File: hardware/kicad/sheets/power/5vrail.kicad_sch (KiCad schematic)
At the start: 11 parts, among them U8 TPSM33625RDNR

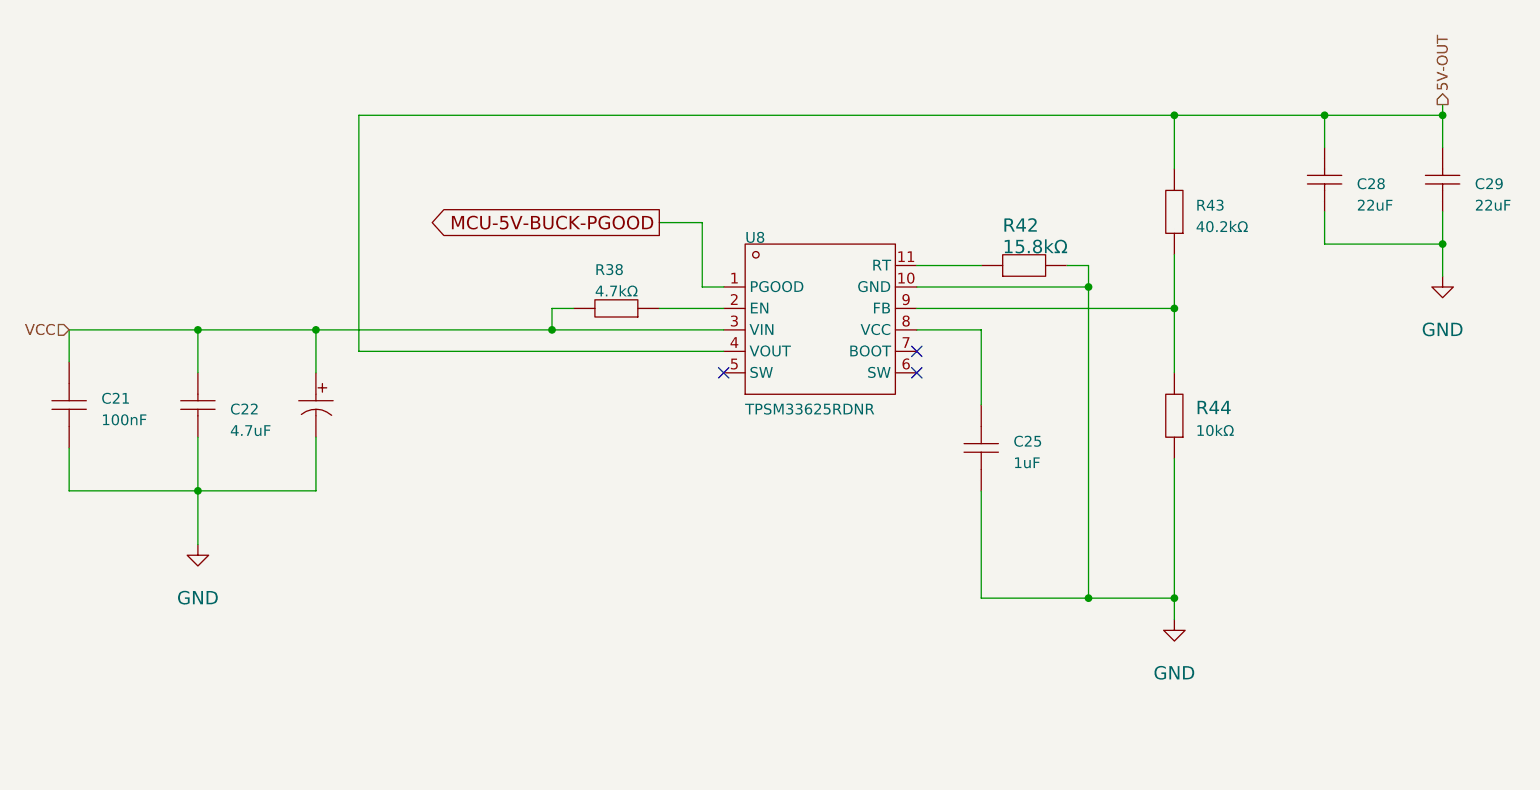
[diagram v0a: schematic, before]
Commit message: resheeted bms and fixed links for the 12v buck
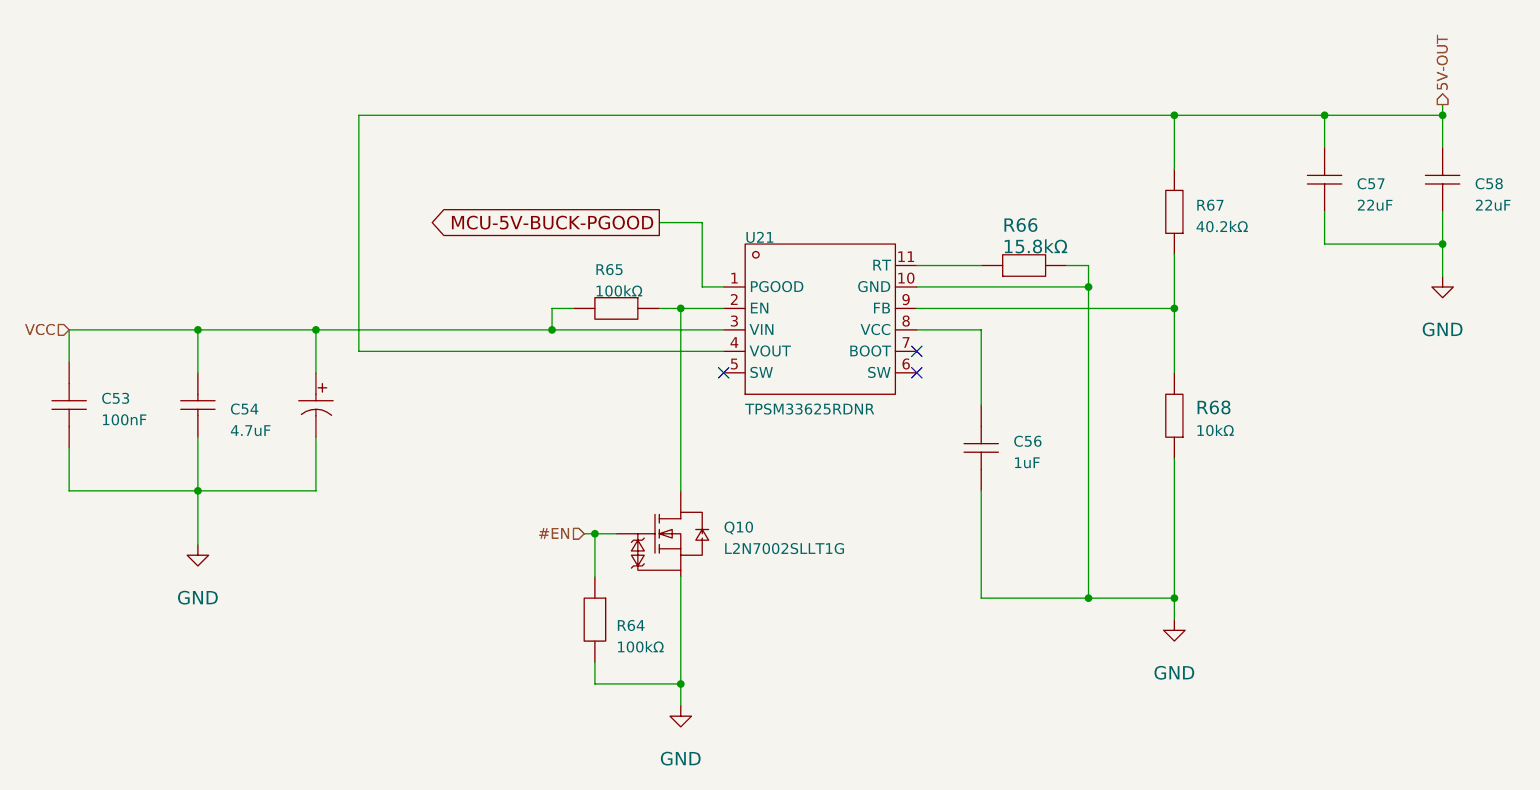
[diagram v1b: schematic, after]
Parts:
- removed R38: 4.7kΩ, Resistor_SMD:R_0603_1608Metric, symbol 5v rail sm-easyedapro:0603WAF4701T5E
- added Q10: L2N7002SLLT1G, Package_TO_SOT_SMD:SOT-23, symbol 5v rail sm-easyedapro:L2N7002SLLT1G
- added R64, R65: 100kΩ, Resistor_SMD:R_0603_1608Metric, symbol 5v rail sm-easyedapro:FRC0603J104 TS
- renumbered C21 to C53, C22 to C54, C23 to C55, C25 to C56, C28 to C57, C29 to C58, R42 to R66, R43 to R67, R44 to R68, U8 to U21
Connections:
- net GND: now also Q10.2 (S), R64.2
- net VCC: now also R65.2
- net at U21.2 (EN): now also Q10.3 (D), R65.1
- new net #EN: Q10.1 (G), R64.1

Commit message: realized having 2 3v3 rails can cause issues
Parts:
- renumbered C53 to C58, C54 to C59, C55 to C60, C56 to C61, C57 to C62, C58 to C63, Q10 to Q2, R64 to R66, R65 to R67, R66 to R68, R67 to R69, R68 to R70, U21 to U23
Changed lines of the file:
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@@
 		(on_board yes)
 		(dnp no)
-		(property "Reference" "C58"
+		(property "Reference" "C63"
 			(at 215.9 68.58 90)
 			(effects
@@
 		(instances
 			(project "svea_powerboard_rev3"
-				(path "/3f85abf4-0b95-4c4a-b7e9-06f59ca1ea3d/5c2e021f-c2d4-49e2-8c36-9a64f1f12002/a68287e1-0132-459f-8ffe-0b4658425697"
-					(reference "C58")
+				(path "/3f85abf4-0b95-4c4a-b7e9-06f59ca1ea3d/5c2e021f-c2d4-49e2-8c36-9a64f1f12001/de8125f2-04ec-46c6-89d6-d0b5e89f6023"
+					(reference "C63")
 					(unit 1)
 				)
@@
 		(on_board yes)
 		(dnp no)
-		(property "Reference" "U21"
+		(property "Reference" "U23"
 			(at 129.54 74.93 0)
 			(effects
@@
 		(instances
 			(project "svea_powerboard_rev3"
-				(path "/3f85abf4-0b95-4c4a-b7e9-06f59ca1ea3d/5c2e021f-c2d4-49e2-8c36-9a64f1f12002/a68287e1-0132-459f-8ffe-0b4658425697"
-					(reference "U21")
+				(path "/3f85abf4-0b95-4c4a-b7e9-06f59ca1ea3d/5c2e021f-c2d4-49e2-8c36-9a64f1f12001/de8125f2-04ec-46c6-89d6-d0b5e89f6023"
+					(reference "U23")
 					(unit 1)
 				)
@@
 		(on_board yes)
 		(dnp no)
-		(property "Reference" "R64"
+		(property "Reference" "R66"
 			(at 114.3 119.38 90)
 			(effects
@@
 		(instances
 			(project "svea_powerboard_rev3"
-				(path "/3f85abf4-0b95-4c4a-b7e9-06f59ca1ea3d/5c2e021f-c2d4-49e2-8c36-9a64f1f12002/a68287e1-0132-459f-8ffe-0b4658425697"
-					(reference "R64")
+				(path "/3f85abf4-0b95-4c4a-b7e9-06f59ca1ea3d/5c2e021f-c2d4-49e2-8c36-9a64f1f12001/de8125f2-04ec-46c6-89d6-d0b5e89f6023"
+					(reference "R66")
 					(unit 1)
 				)
@@
 		(on_board yes)
 		(dnp no)
-		(property "Reference" "Q10"
+		(property "Reference" "Q2"
 			(at 127 109.22 0)
 			(effects
@@
 		(instances
 			(project "svea_powerboard_rev3"
-				(path "/3f85abf4-0b95-4c4a-b7e9-06f59ca1ea3d/5c2e021f-c2d4-49e2-8c36-9a64f1f12002/a68287e1-0132-459f-8ffe-0b4658425697"
-					(reference "Q10")
+				(path "/3f85abf4-0b95-4c4a-b7e9-06f59ca1ea3d/5c2e021f-c2d4-49e2-8c36-9a64f1f12001/de8125f2-04ec-46c6-89d6-d0b5e89f6023"
+					(reference "Q2")
 					(unit 1)
 				)
@@
 		(on_board yes)
 		(dnp no)
-		(property "Reference" "#PWR075"
+		(property "Reference" "#PWR013"
 			(at 212.09 78.74 0)
 			(effects
@@
 		(instances
 			(project "svea_powerboard_rev3"
-				(path "/3f85abf4-0b95-4c4a-b7e9-06f59ca1ea3d/5c2e021f-c2d4-49e2-8c36-9a64f1f12002/a68287e1-0132-459f-8ffe-0b4658425697"
-					(reference "#PWR075")
+				(path "/3f85abf4-0b95-4c4a-b7e9-06f59ca1ea3d/5c2e021f-c2d4-49e2-8c36-9a64f1f12001/de8125f2-04ec-46c6-89d6-d0b5e89f6023"
+					(reference "#PWR013")
 					(unit 1)
 				)
@@
 		(on_board yes)
 		(dnp no)
-		(property "Reference" "C53"
+		(property "Reference" "C58"
 			(at 53.34 93.98 90)
 			(effects
@@
 		(instances
 			(project "svea_powerboard_rev3"
-				(path "/3f85abf4-0b95-4c4a-b7e9-06f59ca1ea3d/5c2e021f-c2d4-49e2-8c36-9a64f1f12002/a68287e1-0132-459f-8ffe-0b4658425697"
-					(reference "C53")
+				(path "/3f85abf4-0b95-4c4a-b7e9-06f59ca1ea3d/5c2e021f-c2d4-49e2-8c36-9a64f1f12001/de8125f2-04ec-46c6-89d6-d0b5e89f6023"
+					(reference "C58")
 					(unit 1)
 				)
@@
 		(on_board yes)
 		(dnp no)
-		(property "Reference" "R67"
+		(property "Reference" "R69"
 			(at 182.88 71.12 90)
 			(effects
@@
 		(instances
 			(project "svea_powerboard_rev3"
-				(path "/3f85abf4-0b95-4c4a-b7e9-06f59ca1ea3d/5c2e021f-c2d4-49e2-8c36-9a64f1f12002/a68287e1-0132-459f-8ffe-0b4658425697"
-					(reference "R67")
+				(path "/3f85abf4-0b95-4c4a-b7e9-06f59ca1ea3d/5c2e021f-c2d4-49e2-8c36-9a64f1f12001/de8125f2-04ec-46c6-89d6-d0b5e89f6023"
+					(reference "R69")
 					(unit 1)
 				)
@@
 		(on_board yes)
 		(dnp no)
-		(property "Reference" "C56"
+		(property "Reference" "C61"
 			(at 161.29 99.06 90)
 			(effects
@@
 		(instances
 			(project "svea_powerboard_rev3"
-				(path "/3f85abf4-0b95-4c4a-b7e9-06f59ca1ea3d/5c2e021f-c2d4-49e2-8c36-9a64f1f12002/a68287e1-0132-459f-8ffe-0b4658425697"
-					(reference "C56")
+				(path "/3f85abf4-0b95-4c4a-b7e9-06f59ca1ea3d/5c2e021f-c2d4-49e2-8c36-9a64f1f12001/de8125f2-04ec-46c6-89d6-d0b5e89f6023"
+					(reference "C61")
 					(unit 1)
 				)
@@
 		(on_board yes)
 		(dnp no)
-		(property "Reference" "#PWR074"
+		(property "Reference" "#PWR012"
 			(at 180.34 119.38 0)
 			(effects
@@
 		(instances
 			(project "svea_powerboard_rev3"
-				(path "/3f85abf4-0b95-4c4a-b7e9-06f59ca1ea3d/5c2e021f-c2d4-49e2-8c36-9a64f1f12002/a68287e1-0132-459f-8ffe-0b4658425697"
-					(reference "#PWR074")
+				(path "/3f85abf4-0b95-4c4a-b7e9-06f59ca1ea3d/5c2e021f-c2d4-49e2-8c36-9a64f1f12001/de8125f2-04ec-46c6-89d6-d0b5e89f6023"
+					(reference "#PWR012")
 					(unit 1)
 				)
@@
 		(on_board yes)
 		(dnp no)
-		(property "Reference" "#PWR073"
+		(property "Reference" "#PWR011"
 			(at 121.92 129.54 0)
 			(effects
@@
 		(instances
 			(project "svea_powerboard_rev3"
-				(path "/3f85abf4-0b95-4c4a-b7e9-06f59ca1ea3d/5c2e021f-c2d4-49e2-8c36-9a64f1f12002/a68287e1-0132-459f-8ffe-0b4658425697"
-					(reference "#PWR073")
+				(path "/3f85abf4-0b95-4c4a-b7e9-06f59ca1ea3d/5c2e021f-c2d4-49e2-8c36-9a64f1f12001/de8125f2-04ec-46c6-89d6-d0b5e89f6023"
+					(reference "#PWR011")
 					(unit 1)
 				)
@@
 		(on_board yes)
 		(dnp no)
-		(property "Reference" "R66"
+		(property "Reference" "R68"
 			(at 160.02 73.66 0)
 			(effects
@@
 		(instances
 			(project "svea_powerboard_rev3"
-				(path "/3f85abf4-0b95-4c4a-b7e9-06f59ca1ea3d/5c2e021f-c2d4-49e2-8c36-9a64f1f12002/a68287e1-0132-459f-8ffe-0b4658425697"
-					(reference "R66")
+				(path "/3f85abf4-0b95-4c4a-b7e9-06f59ca1ea3d/5c2e021f-c2d4-49e2-8c36-9a64f1f12001/de8125f2-04ec-46c6-89d6-d0b5e89f6023"
+					(reference "R68")
 					(unit 1)
 				)
@@
 		(on_board yes)
 		(dnp no)
-		(property "Reference" "R65"
+		(property "Reference" "R67"
 			(at 111.76 78.74 0)
 			(effects
@@
 		(instances
 			(project "svea_powerboard_rev3"
-				(path "/3f85abf4-0b95-4c4a-b7e9-06f59ca1ea3d/5c2e021f-c2d4-49e2-8c36-9a64f1f12002/a68287e1-0132-459f-8ffe-0b4658425697"
-					(reference "R65")
+				(path "/3f85abf4-0b95-4c4a-b7e9-06f59ca1ea3d/5c2e021f-c2d4-49e2-8c36-9a64f1f12001/de8125f2-04ec-46c6-89d6-d0b5e89f6023"
+					(reference "R67")
 					(unit 1)
 				)
@@
 		(on_board yes)
 		(dnp no)
-		(property "Reference" "C57"
+		(property "Reference" "C62"
 			(at 201.93 68.58 90)
 			(effects
@@
 		(instances
 			(project "svea_powerboard_rev3"
-				(path "/3f85abf4-0b95-4c4a-b7e9-06f59ca1ea3d/5c2e021f-c2d4-49e2-8c36-9a64f1f12002/a68287e1-0132-459f-8ffe-0b4658425697"
-					(reference "C57")
+				(path "/3f85abf4-0b95-4c4a-b7e9-06f59ca1ea3d/5c2e021f-c2d4-49e2-8c36-9a64f1f12001/de8125f2-04ec-46c6-89d6-d0b5e89f6023"
+					(reference "C62")
 					(unit 1)
 				)
@@
 		(on_board yes)
 		(dnp no)
-		(property "Reference" "C54"
+		(property "Reference" "C59"
 			(at 68.58 95.25 90)
 			(effects
@@
 		(instances
 			(project "svea_powerboard_rev3"
-				(path "/3f85abf4-0b95-4c4a-b7e9-06f59ca1ea3d/5c2e021f-c2d4-49e2-8c36-9a64f1f12002/a68287e1-0132-459f-8ffe-0b4658425697"
-					(reference "C54")
+				(path "/3f85abf4-0b95-4c4a-b7e9-06f59ca1ea3d/5c2e021f-c2d4-49e2-8c36-9a64f1f12001/de8125f2-04ec-46c6-89d6-d0b5e89f6023"
+					(reference "C59")
 					(unit 1)
 				)
@@
 		(on_board yes)
 		(dnp no)
-		(property "Reference" "#PWR072"
+		(property "Reference" "#PWR09"
 			(at 64.77 110.49 0)
 			(effects
@@
 		(instances
 			(project "svea_powerboard_rev3"
-				(path "/3f85abf4-0b95-4c4a-b7e9-06f59ca1ea3d/5c2e021f-c2d4-49e2-8c36-9a64f1f12002/a68287e1-0132-459f-8ffe-0b4658425697"
-					(reference "#PWR072")
+				(path "/3f85abf4-0b95-4c4a-b7e9-06f59ca1ea3d/5c2e021f-c2d4-49e2-8c36-9a64f1f12001/de8125f2-04ec-46c6-89d6-d0b5e89f6023"
+					(reference "#PWR09")
 					(unit 1)
 				)
@@
 		(on_board yes)
 		(dnp no)
-		(property "Reference" "R68"
+		(property "Reference" "R70"
 			(at 182.88 95.25 90)
 			(effects
@@
 		(instances
 			(project "svea_powerboard_rev3"
-				(path "/3f85abf4-0b95-4c4a-b7e9-06f59ca1ea3d/5c2e021f-c2d4-49e2-8c36-9a64f1f12002/a68287e1-0132-459f-8ffe-0b4658425697"
-					(reference "R68")
+				(path "/3f85abf4-0b95-4c4a-b7e9-06f59ca1ea3d/5c2e021f-c2d4-49e2-8c36-9a64f1f12001/de8125f2-04ec-46c6-89d6-d0b5e89f6023"
+					(reference "R70")
 					(unit 1)
 				)
@@
 		(on_board yes)
 		(dnp no)
-		(property "Reference" "C55"
+		(property "Reference" "C60"
 			(at 82.55 93.98 90)
 			(effects
@@
 		(instances
 			(project "svea_powerboard_rev3"
-				(path "/3f85abf4-0b95-4c4a-b7e9-06f59ca1ea3d/5c2e021f-c2d4-49e2-8c36-9a64f1f12002/a68287e1-0132-459f-8ffe-0b4658425697"
-					(reference "C55")
+				(path "/3f85abf4-0b95-4c4a-b7e9-06f59ca1ea3d/5c2e021f-c2d4-49e2-8c36-9a64f1f12001/de8125f2-04ec-46c6-89d6-d0b5e89f6023"
+					(reference "C60")
 					(unit 1)
 				)

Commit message: various improvements
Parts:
- renumbered C58 to C82, C59 to C83, C60 to C84, C61 to C85, C62 to C86, C63 to C87, Q2 to Q16, R66 to R90, R67 to R91, R68 to R92, R69 to R93, R70 to R94, U23 to U44
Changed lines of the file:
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@@
 		(on_board yes)
 		(dnp no)
-		(property "Reference" "C63"
+		(property "Reference" "C87"
 			(at 215.9 68.58 90)
 			(effects
@@
 			(project "svea_powerboard_rev3"
 				(path "/3f85abf4-0b95-4c4a-b7e9-06f59ca1ea3d/5c2e021f-c2d4-49e2-8c36-9a64f1f12001/de8125f2-04ec-46c6-89d6-d0b5e89f6023"
-					(reference "C63")
+					(reference "C87")
 					(unit 1)
 				)
@@
 		(on_board yes)
 		(dnp no)
-		(property "Reference" "U23"
+		(property "Reference" "U44"
 			(at 129.54 74.93 0)
 			(effects
@@
 			(project "svea_powerboard_rev3"
 				(path "/3f85abf4-0b95-4c4a-b7e9-06f59ca1ea3d/5c2e021f-c2d4-49e2-8c36-9a64f1f12001/de8125f2-04ec-46c6-89d6-d0b5e89f6023"
-					(reference "U23")
+					(reference "U44")
 					(unit 1)
 				)
@@
 		(on_board yes)
 		(dnp no)
-		(property "Reference" "R66"
+		(property "Reference" "R90"
 			(at 114.3 119.38 90)
 			(effects
@@
 			(project "svea_powerboard_rev3"
 				(path "/3f85abf4-0b95-4c4a-b7e9-06f59ca1ea3d/5c2e021f-c2d4-49e2-8c36-9a64f1f12001/de8125f2-04ec-46c6-89d6-d0b5e89f6023"
-					(reference "R66")
+					(reference "R90")
 					(unit 1)
 				)
@@
 		(on_board yes)
 		(dnp no)
-		(property "Reference" "Q2"
+		(property "Reference" "Q16"
 			(at 127 109.22 0)
 			(effects
@@
 			(project "svea_powerboard_rev3"
 				(path "/3f85abf4-0b95-4c4a-b7e9-06f59ca1ea3d/5c2e021f-c2d4-49e2-8c36-9a64f1f12001/de8125f2-04ec-46c6-89d6-d0b5e89f6023"
-					(reference "Q2")
+					(reference "Q16")
 					(unit 1)
 				)
@@
 		(on_board yes)
 		(dnp no)
-		(property "Reference" "#PWR013"
+		(property "Reference" "#PWR0139"
 			(at 212.09 78.74 0)
 			(effects
@@
 			(project "svea_powerboard_rev3"
 				(path "/3f85abf4-0b95-4c4a-b7e9-06f59ca1ea3d/5c2e021f-c2d4-49e2-8c36-9a64f1f12001/de8125f2-04ec-46c6-89d6-d0b5e89f6023"
-					(reference "#PWR013")
+					(reference "#PWR0139")
 					(unit 1)
 				)
@@
 		(on_board yes)
 		(dnp no)
-		(property "Reference" "C58"
+		(property "Reference" "C82"
 			(at 53.34 93.98 90)
 			(effects
@@
 			(project "svea_powerboard_rev3"
 				(path "/3f85abf4-0b95-4c4a-b7e9-06f59ca1ea3d/5c2e021f-c2d4-49e2-8c36-9a64f1f12001/de8125f2-04ec-46c6-89d6-d0b5e89f6023"
-					(reference "C58")
+					(reference "C82")
 					(unit 1)
 				)
@@
 		(on_board yes)
 		(dnp no)
-		(property "Reference" "R69"
+		(property "Reference" "R93"
 			(at 182.88 71.12 90)
 			(effects
@@
 			(project "svea_powerboard_rev3"
 				(path "/3f85abf4-0b95-4c4a-b7e9-06f59ca1ea3d/5c2e021f-c2d4-49e2-8c36-9a64f1f12001/de8125f2-04ec-46c6-89d6-d0b5e89f6023"
-					(reference "R69")
+					(reference "R93")
 					(unit 1)
 				)
@@
 		(on_board yes)
 		(dnp no)
-		(property "Reference" "C61"
+		(property "Reference" "C85"
 			(at 161.29 99.06 90)
 			(effects
@@
 			(project "svea_powerboard_rev3"
 				(path "/3f85abf4-0b95-4c4a-b7e9-06f59ca1ea3d/5c2e021f-c2d4-49e2-8c36-9a64f1f12001/de8125f2-04ec-46c6-89d6-d0b5e89f6023"
-					(reference "C61")
+					(reference "C85")
 					(unit 1)
 				)
@@
 		(on_board yes)
 		(dnp no)
-		(property "Reference" "#PWR012"
+		(property "Reference" "#PWR0138"
 			(at 180.34 119.38 0)
 			(effects
@@
 			(project "svea_powerboard_rev3"
 				(path "/3f85abf4-0b95-4c4a-b7e9-06f59ca1ea3d/5c2e021f-c2d4-49e2-8c36-9a64f1f12001/de8125f2-04ec-46c6-89d6-d0b5e89f6023"
-					(reference "#PWR012")
+					(reference "#PWR0138")
 					(unit 1)
 				)
@@
 		(on_board yes)
 		(dnp no)
-		(property "Reference" "#PWR011"
+		(property "Reference" "#PWR0137"
 			(at 121.92 129.54 0)
 			(effects
@@
 			(project "svea_powerboard_rev3"
 				(path "/3f85abf4-0b95-4c4a-b7e9-06f59ca1ea3d/5c2e021f-c2d4-49e2-8c36-9a64f1f12001/de8125f2-04ec-46c6-89d6-d0b5e89f6023"
-					(reference "#PWR011")
+					(reference "#PWR0137")
 					(unit 1)
 				)
@@
 		(on_board yes)
 		(dnp no)
-		(property "Reference" "R68"
+		(property "Reference" "R92"
 			(at 160.02 73.66 0)
 			(effects
@@
 			(project "svea_powerboard_rev3"
 				(path "/3f85abf4-0b95-4c4a-b7e9-06f59ca1ea3d/5c2e021f-c2d4-49e2-8c36-9a64f1f12001/de8125f2-04ec-46c6-89d6-d0b5e89f6023"
-					(reference "R68")
+					(reference "R92")
 					(unit 1)
 				)
@@
 		(on_board yes)
 		(dnp no)
-		(property "Reference" "R67"
+		(property "Reference" "R91"
 			(at 111.76 78.74 0)
 			(effects
@@
 			(project "svea_powerboard_rev3"
 				(path "/3f85abf4-0b95-4c4a-b7e9-06f59ca1ea3d/5c2e021f-c2d4-49e2-8c36-9a64f1f12001/de8125f2-04ec-46c6-89d6-d0b5e89f6023"
-					(reference "R67")
+					(reference "R91")
 					(unit 1)
 				)
@@
 		(on_board yes)
 		(dnp no)
-		(property "Reference" "C62"
+		(property "Reference" "C86"
 			(at 201.93 68.58 90)
 			(effects
@@
 			(project "svea_powerboard_rev3"
 				(path "/3f85abf4-0b95-4c4a-b7e9-06f59ca1ea3d/5c2e021f-c2d4-49e2-8c36-9a64f1f12001/de8125f2-04ec-46c6-89d6-d0b5e89f6023"
-					(reference "C62")
+					(reference "C86")
 					(unit 1)
 				)
@@
 		(on_board yes)
 		(dnp no)
-		(property "Reference" "C59"
+		(property "Reference" "C83"
 			(at 68.58 95.25 90)
 			(effects
@@
 			(project "svea_powerboard_rev3"
 				(path "/3f85abf4-0b95-4c4a-b7e9-06f59ca1ea3d/5c2e021f-c2d4-49e2-8c36-9a64f1f12001/de8125f2-04ec-46c6-89d6-d0b5e89f6023"
-					(reference "C59")
+					(reference "C83")
 					(unit 1)
 				)
@@
 		(on_board yes)
 		(dnp no)
-		(property "Reference" "#PWR09"
+		(property "Reference" "#PWR0136"
 			(at 64.77 110.49 0)
 			(effects
@@
 			(project "svea_powerboard_rev3"
 				(path "/3f85abf4-0b95-4c4a-b7e9-06f59ca1ea3d/5c2e021f-c2d4-49e2-8c36-9a64f1f12001/de8125f2-04ec-46c6-89d6-d0b5e89f6023"
-					(reference "#PWR09")
+					(reference "#PWR0136")
 					(unit 1)
 				)
@@
 		(on_board yes)
 		(dnp no)
-		(property "Reference" "R70"
+		(property "Reference" "R94"
 			(at 182.88 95.25 90)
 			(effects
@@
 			(project "svea_powerboard_rev3"
 				(path "/3f85abf4-0b95-4c4a-b7e9-06f59ca1ea3d/5c2e021f-c2d4-49e2-8c36-9a64f1f12001/de8125f2-04ec-46c6-89d6-d0b5e89f6023"
-					(reference "R70")
+					(reference "R94")
 					(unit 1)
 				)
@@
 		(on_board yes)
 		(dnp no)
-		(property "Reference" "C60"
+		(property "Reference" "C84"
 			(at 82.55 93.98 90)
 			(effects
@@
 			(project "svea_powerboard_rev3"
 				(path "/3f85abf4-0b95-4c4a-b7e9-06f59ca1ea3d/5c2e021f-c2d4-49e2-8c36-9a64f1f12001/de8125f2-04ec-46c6-89d6-d0b5e89f6023"
-					(reference "C60")
+					(reference "C84")
 					(unit 1)
 				)
